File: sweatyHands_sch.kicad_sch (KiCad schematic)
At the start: 69 parts, among them J2 Conn_01x04_Socket, J3 Conn_02x06_Odd_Even, J4 Barrel_Jack, J5 USB_C_Receptacle_USB2.0_16P, J7 Conn_01x02_Socket, Q1 UMH3N, Q2 2N2222, Q3 AO3400A, Q4 DMG2305UX-13, Q5 DMG2305UX-13, Q6 AO3400A, SW1 SW_SPST, U1 ESP32-WROOM-32E, U2 TPS54202DDCT, U4 TLV1117LV-3.3, U5 TPS2116DRL, U6 TPS2553DBVR, U7 CP2104, U8 USBLC6-2SC6

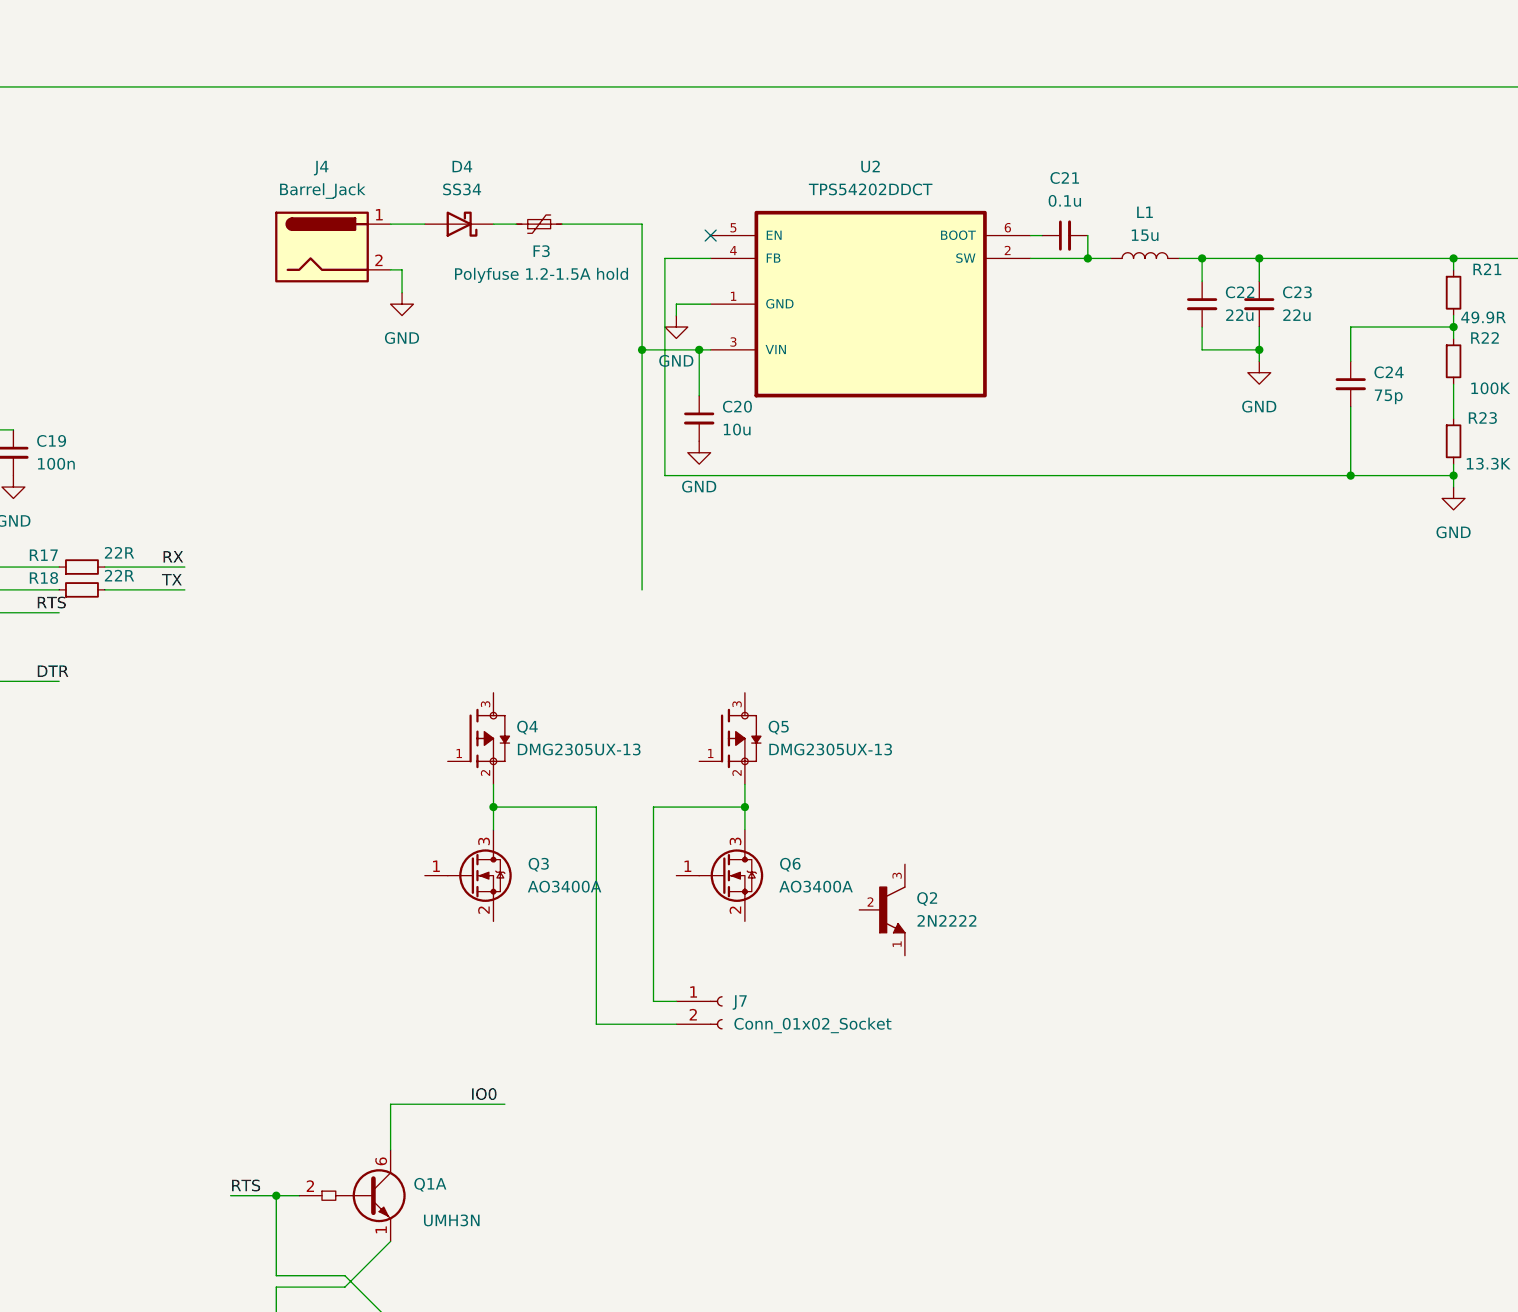
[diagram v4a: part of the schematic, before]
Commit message: Almost done with Hbridge
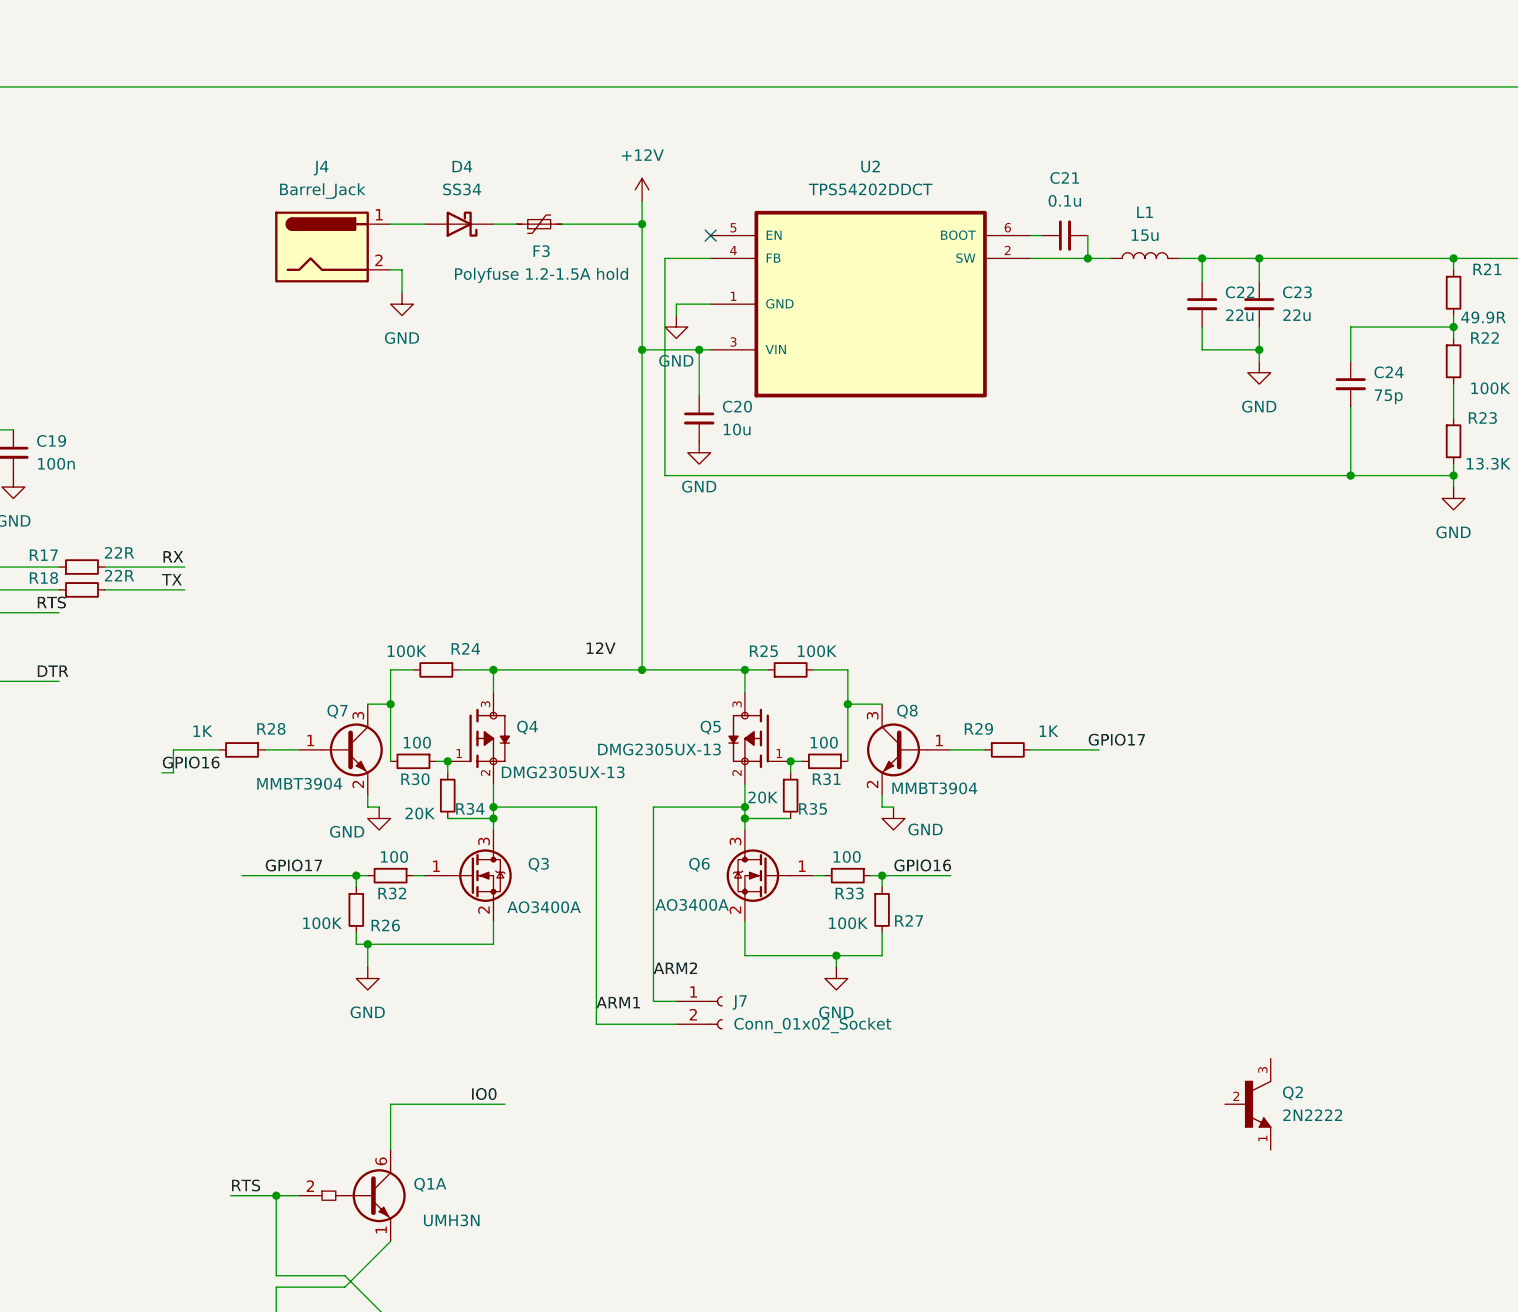
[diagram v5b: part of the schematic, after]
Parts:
- added Q7, Q8: MMBT3904, Package_TO_SOT_SMD:SOT-23, symbol Transistor_BJT:MMBT3904
- added R24, R25, R26, R27: 100K, symbol Device:R_Small
- added R28, R29: 1K, symbol Device:R_Small
- added R30, R31, R32, R33: 100, symbol Device:R_Small
- added R34, R35: 20K, symbol Device:R_Small
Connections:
- net GND: now also Q3.2 (S), Q6.2 (S), Q7.2 (E), Q8.2 (E), R26.2, R27.2
- net GPIO16: now also R27.1, R28.2, R33.1
- net GPIO17: now also R26.1, R29.2, R32.2
- net at Q3.1 (G): now also R32.1
- net ARM1: now reaches J7.2 (Pin_2), Q3.3 (D), Q4.2
- net ARM1: now also R34.2
- net +12V: now reaches C20.1, F3.2, U2.3 (VIN)
- net +12V: now also Q4.3, Q5.3, R24.1, R25.1
- net at Q6.1 (G): now also R33.2
- net ARM2: now reaches J7.1 (Pin_1), Q5.2, Q6.3 (D)
- net ARM2: now also R35.2
- net at Q5.1: now also R31.2, R35.1
- net at Q4.1: now also R30.1, R34.1
- new net: Q8.1 (B), R29.1
- new net: Q7.1 (B), R28.1
- new net: Q7.3 (C), R24.2, R30.2
- new net: Q8.3 (C), R25.2, R31.1
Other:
- moved on the sheet: Q2, Q5, Q6

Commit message: Finished Schem
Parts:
- removed 47K: 1K, symbol Device:R_Small
- removed FB2, FB3: MPZ2012S221AT000, symbol Device:FerriteBead_Small
- removed Q2: 2N2222, 2N2222:TO127P580H530-3, symbol 2N2222:2N2222
- added CR1, CR2: MMSZ5236B-7-F, SOD123_DIO, symbol Zener:MMSZ5236B-7-F
- added L2, L3: MPZ2012S221AT000, IND_2012_TDK, symbol ferrit_bead:MPZ2012S221AT000
- added Q10, Q9: 2N3904, Package_TO_SOT_THT:TO-92_Inline, symbol Transistor_BJT:2N3904
- added R36: 42K, Resistor_SMD:R_0805_2012Metric, symbol Device:R_Small
- added R37: 35, Resistor_SMD:R_0805_2012Metric, symbol Device:R_Small
- added R38: 47K, Resistor_SMD:R_0805_2012Metric, symbol Device:R_Small
- C10, C11, C12, C13, C14, C15, C16, C17, C18, C19, C20, C21, C22, C23, C24, C7, C8, C9: footprint (none) -> Capacitor_SMD:C_0805_2012Metric_Pad1.18x1.45mm_HandSolder
- D1: footprint (none) -> LED_SMD:LED_RGB_Wuerth-PLCC4_3.2x2.8mm_150141M173100
- D2: footprint (none) -> LED_SMD:LED_0603_1608Metric_Pad1.05x0.95mm_HandSolder
- F2, F3: footprint (none) -> Fuse:Fuse_0805_2012Metric_Pad1.15x1.40mm_HandSolder
- H1, H2, H3, H4: footprint (none) -> MountingHole:MountingHole_3.2mm_M3_Pad_Via
- J2: footprint (none) -> Connector_PinHeader_2.54mm:PinHeader_1x04_P2.54mm_Vertical
- J3: footprint (none) -> Connector_PinHeader_2.54mm:PinHeader_2x06_P2.54mm_Vertical
- J4: footprint (none) -> CUI_PJ-002B
- J5: footprint (none) -> Connector_USB:USB_C_Receptacle_Amphenol_12401948E412A
- L1: footprint (none) -> Inductor_SMD:L_0805_2012Metric
- R10, R11, R12, R13, R14, R15, R16, R17, R18, R19, R20, R21, R22, R23, R26, R27, R28, R29, R32, R33, R34, R35, R6, R7, R8, R9: footprint (none) -> Resistor_SMD:R_0805_2012Metric
- R24, R25: value 100K -> 47K; footprint (none) -> Resistor_SMD:R_0805_2012Metric
- R30, R31: value 100 -> 470; footprint (none) -> Resistor_SMD:R_0805_2012Metric
- SW1: footprint (none) -> Button_Switch_SMD:SW_Push_1TS009xxxx-xxxx-xxxx_6x6x5mm
- U2: footprint TPS54202DDCT:SOT95P280X110-6N -> Extra:SOT95P280X110-6N
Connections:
- net +12V: now also R36.1
- net +3.3V: now also R38.1
- net ARM1: now also CR1.1
- net ARM2: now also CR2.1
- net FAULT: now also R38.2
- net GND: now also Q10.1 (E), R37.2; no longer Q3.2 (S), Q6.2 (S), Q7.2 (E), Q8.2 (E), R26.2, R27.2
- net Vout: now also L2.1
- net at U5.3 (VIN1): now also L2.2
- net at U6.6 (OUT): now also L3.2
- net at U5.6 (VIN2): now also L3.1
- net at Q4.1, R30.1, R34.1: now also CR1.2
- new net: Q10.2 (B), Q9.1 (E), R37.1
- new net: Q10.3 (C), Q9.2 (B), R36.2
- new net Digi_GND: Q3.2 (S), Q6.2 (S), Q7.2 (E), Q8.2 (E), Q9.3 (C), R26.2, R27.2
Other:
- moved on the sheet: J7, Q1A, Q1B, Q3, Q6, Q7, Q8, R26, R27, R28, R29, R30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

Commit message: Meow
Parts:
- removed C20: 10u, Capacitor_SMD:C_0805_2012Metric_Pad1.18x1.45mm_HandSolder, symbol Device:C_Small
- removed C21: 0.1u, Capacitor_SMD:C_0805_2012Metric_Pad1.18x1.45mm_HandSolder, symbol Device:C_Small
- removed C22, C23: 22u, Capacitor_SMD:C_0805_2012Metric_Pad1.18x1.45mm_HandSolder, symbol Device:C_Small
- removed C24: 75p, Capacitor_SMD:C_0805_2012Metric_Pad1.18x1.45mm_HandSolder, symbol Device:C_Small
- removed CR1, CR2: MMSZ5236B-7-F, SOD123_DIO, symbol Zener:MMSZ5236B-7-F
- removed D3: PESD5V0S1UL_315, PESD5V0S1UL_315:DIO_PESD5V0S1UL_315, symbol PESD5V0S1UL_315:PESD5V0S1UL_315
- removed D4: SS34, Diode_SMD:D_SMA, symbol Diode:SS34
- removed J7: Conn_01x02_Socket, Connector:Banana_Jack_2Pin, symbol Connector:Conn_01x02_Socket
- removed L1: 15u, Inductor_SMD:L_0805_2012Metric, symbol Device:L
- removed Q10, Q9: 2N3904, Package_TO_SOT_THT:TO-92_Inline, symbol Transistor_BJT:2N3904
- removed Q3, Q6: AO3400A, Package_TO_SOT_SMD:SOT-23, symbol Transistor_FET:AO3400A
- removed Q4, Q5: DMG2305UX-13, DMG2305UX-13:SOT91P240X110-3N, symbol DMG2305UX-13:DMG2305UX-13
- removed Q7, Q8: MMBT3904, Package_TO_SOT_SMD:SOT-23, symbol Transistor_BJT:MMBT3904
- removed R28: 1K, Resistor_SMD:R_0805_2012Metric, symbol Device:R_Small
- removed U2: TPS54202DDCT, Extra:SOT95P280X110-6N, symbol TPS54202DDCT:TPS54202DDCT
- added C1: 0.1u, symbol Device:C_Small
- added C2, C3: 1u, symbol Device:C_Small
- added C25: 10u, Capacitor_SMD:C_0805_2012Metric_Pad1.18x1.45mm_HandSolder, symbol Device:C_Small
- added C26, C27: 22u, Capacitor_SMD:C_0805_2012Metric_Pad1.18x1.45mm_HandSolder, symbol Device:C_Small
- added C28: 22n, Capacitor_SMD:C_0805_2012Metric_Pad1.18x1.45mm_HandSolder, symbol Device:C_Small
- added C29: 0.1u, Capacitor_SMD:C_0805_2012Metric_Pad1.18x1.45mm_HandSolder, symbol Device:C_Small
- added CR1: SMF36CA, SOD-123F_LTF, symbol TVS40Br:SMF36CA
- added D3, D4: TFZVTR10B, symbol Device:D_Zener
- added D5: PESD5V0S1UL_315, Extra:DIO_PESD5V0S1UL_315, symbol PESD5V0S1UL_315:PESD5V0S1UL_315
- added J1, J6: 105-1103-001, CONN_105-1102-001, symbol bananajack:105-1103-001
- added L4: 5.5u, Inductor_SMD:L_0805_2012Metric, symbol Device:L
- added Q10, Q11: Q_NPN, symbol Device:Q_NPN
- added Q2, Q3, Q4, Q5: AON6266E, symbol Simulation_SPICE:NMOS
- added Q6, Q7: FDC5614P, symbol Simulation_SPICE:PMOS
- added R39: 240K, Resistor_SMD:R_0805_2012Metric, symbol Device:R_Small
- added R40: 100K, Resistor_SMD:R_0805_2012Metric, symbol Device:R_Small
- added R41: 10K, Resistor_SMD:R_0805_2012Metric, symbol Device:R_Small
- added R42: 22K, Resistor_SMD:R_0805_2012Metric, symbol Device:R_Small
- added R43: 24, Resistor_SMD:R_0805_2012Metric, symbol Device:R_Small
- added U3: LMR14020SDDAR, DDA0008E_N, symbol LMR14020SDDAR:LMR14020SDDAR
- R15: value 59K 1% -> 45K 1%
- R21: value 49.9R -> 100R
- R22: value 100K -> 100R
- R23: value 13.3K -> 100R
- R24: value 47K -> 24K
- R25: value 47K -> 100K
- R26: value 100K -> 17.6K
- R29: value 1K -> 100K
- R30: value 470 -> 100K
- R31: value 470 -> 10K
- R32: value 100 -> 10K
- R33: value 100 -> 100R
- R34, R35: value 20K -> 10K
- R36: value 42K -> 10K
- R37: value 35 -> 10K
- U6: footprint TPS2553DBVR:SOT95P280X145-6N -> Extra:SOT95P280X145-6N
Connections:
- net +3.3VA is gone; now on net +3.3V: C18.1, C19.1, R16.1, U7.5 (VIO), U7.6 (VDD)
- net ARM1 is gone; now on net Digi_GND: R34.2
- net ARM2 is gone; now on net Digi_GND: R35.2
- net +3.3V: now also R41.1
- net Digi_GND: now also R21.1, R22.2, R23.1, R33.2, R34.1, R35.1, R36.1, R36.2, R37.1, R37.2, U1.27 (IO16), U1.28 (IO17), Q10.C, Q2.3 (S), Q3.3 (S), Q4.3 (S), Q5.3 (S); no longer R26.2, R27.2
- net GND: now also R24.2, R26.2, U4.1 (GND), U5.1 (GND), C1.2, C2.2, C25.2, C26.2, C27.2, C28.2, C3.2, CR1.2, D5.K, Q11.E, R40.2, R43.2, U3.7 (GND), U3.9 (PAD); no longer R23.2, R37.2
- net GPIO34: no longer U1.6 (IO34)
- net RX: now also U1.34 (RXD0/IO3); no longer U1.35 (TXD0/IO1)
- net TX: now also U1.35 (TXD0/IO1); no longer U1.34 (RXD0/IO3)
- net Vout: now also R25.1, C26.1, C27.1, L4.2; no longer R21.1
- net at R32.1: now also R29.2, D3.2 (A), Q6.2 (G)
- net D_P: now reaches U7.3 (D+), U8.6 (I/O1)
- net D+: now reaches U8.1 (I/O1)
- net D+: now also J5.A6 (D+); no longer U7.4 (D-)
- net +5VP: now reaches J5.A4 (VBUS), J5.A9 (VBUS), J5.B4 (VBUS), J5.B9 (VBUS)
- net +5VP: now also F2.1, D5.A
- net at R22.1: now also Q5.2 (G); no longer R21.2
- net at F3.1: now also J4.1, CR1.1
- net at R31.2: now also Q4.1 (D); no longer R35.1
- net at F2.2, R13.1, U6.1 (IN): now also C1.1
- net +30V: now reaches R29.1
- net +30V: now also F3.2, R27.1, R30.1, C25.1, D3.1 (K), D4.1 (K), Q6.3 (S), Q7.3 (S), R42.1, U3.2 (VIN)
- net at R30.2: now also R31.1, D4.2 (A), Q7.2 (G); no longer R24.2
- net at R25.2: now also R26.1, U3.5 (FB); no longer R31.1
- net D-: now reaches J5.A7 (D-), U8.3 (I/O2)
- net D-: no longer J5.B7 (D-)
- net at L3.1, U5.6 (VIN2): now also C3.1
- net at L2.2, U5.3 (VIN1): now also U5.5 (MODE), C2.1, R39.1
- net at U5.4 (PR1): now also R39.2, R40.1
- net power_mux: now reaches U5.8 (ST)
- net power_mux: now also U1.6 (IO34), R41.2
- removed net +12V: F3.2, R24.1, R25.1, R36.1
- removed net GPIO16: R27.1, R33.1, U1.27 (IO16)
- removed net GPIO17: R26.1, R29.2, R32.2, U1.28 (IO17)
- new net: R27.2, U3.3 (EN)
- new net: Q2.1 (D), R32.2
- new net: Q2.2 (G), R23.2
- new net: R24.1, U3.4 (RT_SYNC)
- new net: Q10.E, Q11.B, R43.1
- new net: C28.1, U3.6 (SS)
- new net: C29.1, L4.1, U3.8 (SW)
- new net: C29.2, U3.1 (BOOT)
- new net: Q3.2 (G), R21.2
- new net: Q10.B, Q11.C, R42.2
- new net: Q4.2 (G), R33.1
- new net D_N: U7.4 (D-), U8.4 (I/O2)
- new net LEFT_HAND: J6.1, J6.2, Q3.1 (D), Q6.1 (D)
- new net RIGHT_HAND: J1.1, J1.2, Q5.1 (D), Q7.1 (D)
- now unconnected: J5.B6 (D+)
- no-connect marks 7 -> 6
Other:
- moved on the sheet: F2, H1, H2, H3, H4, U8
